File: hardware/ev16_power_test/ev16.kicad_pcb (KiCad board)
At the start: 4 copper layers, 125 x 80 mm, 185 parts, among them CN1 Conn_05x02_Female, CN2 PJ-242, J1 USB_C_Receptacle, J10 Conn_01x03_Pin, J11 Conn_02x05_Counter_Clockwise, J2 Conn_01x02_Socket, J3 AudioJack4, J4 Conn_02x03_Odd_Even, J5 Conn_02x03_Odd_Even, J6 Conn_02x05_Counter_Clockwise, J7 Conn_02x05_Counter_Clockwise, J8 Conn_02x05_Counter_Clockwise, J9 Conn_02x05_Counter_Clockwise, Q1 2N7002, Q2 2N7002, Q3 2N7002, SW1 SW_SPDT, SW2 SW_Push, SW3 SW_Push, SW4 SW_Push, SW5 SW_Push, SW6 SW_Push, SW7 SW_Push, U1 BQ21040DBV, U10 STM32F405RGTx, U11 ME6211C28M5, U2 USBLC6-2P6, U3 STM32F072CBTx, U4 CH340C, U5 TPS63060, U6 WM8960CGEFL/RV, U7 ESP32-S3-WROOM-1, U8 M24C02-RMN6TP, U9 TPS2116DRL, Y1 Crystal_GND24

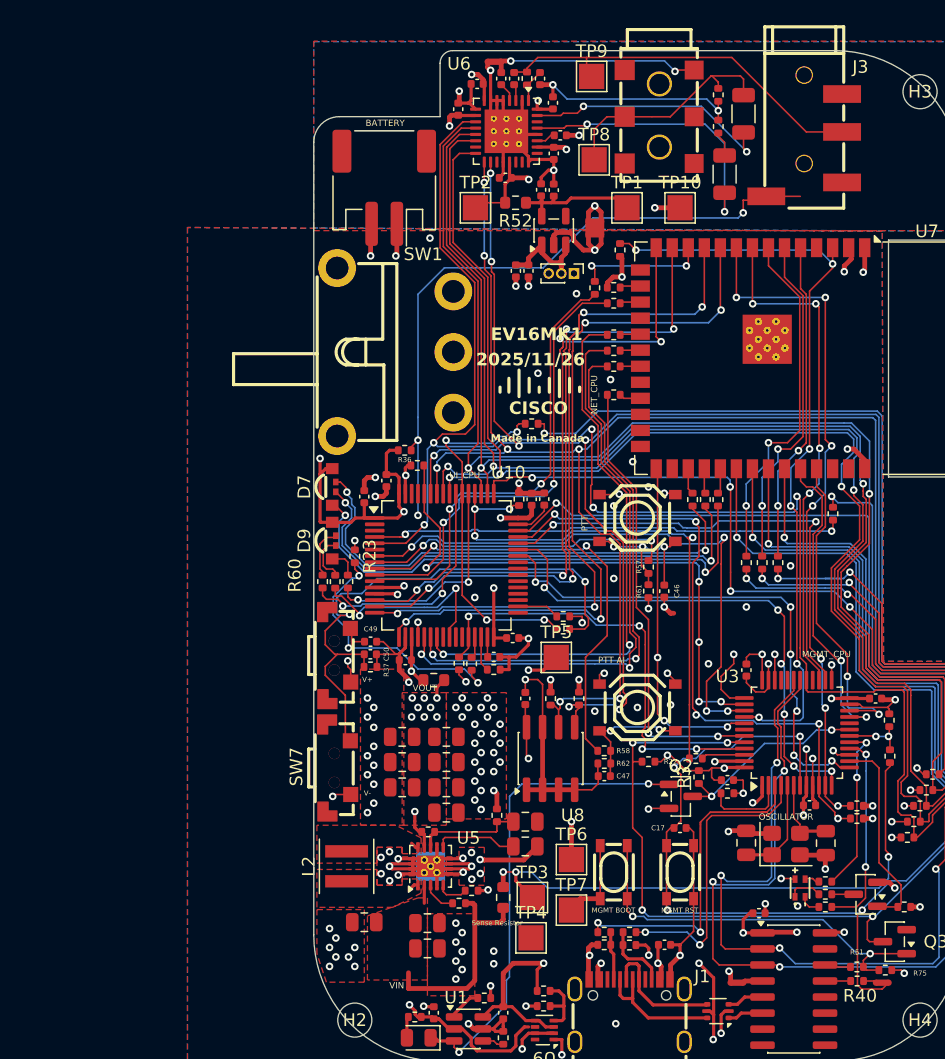
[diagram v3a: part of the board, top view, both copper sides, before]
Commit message: Changed linear regulator to XC6227C301MR-G and made a symbol for it. Added heat sink areas for the analog regulator
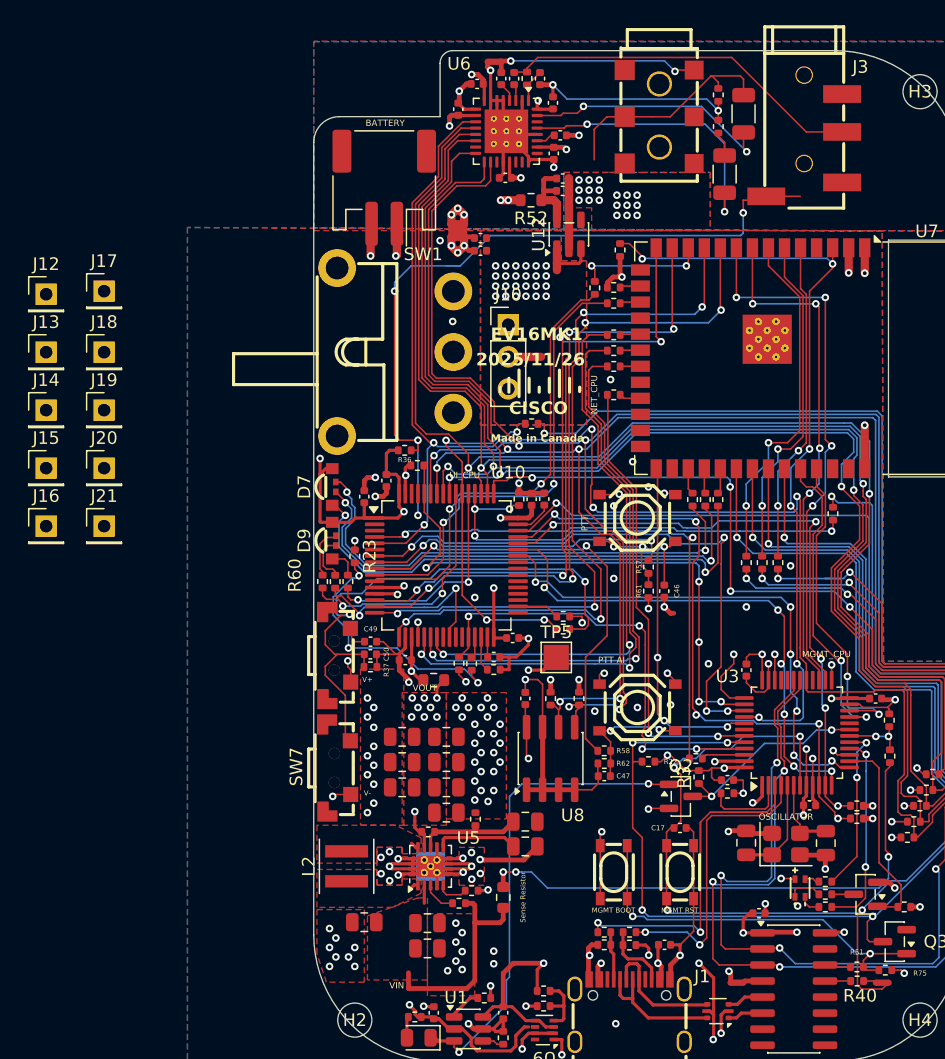
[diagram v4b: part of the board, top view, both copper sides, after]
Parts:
- removed TP1, TP10, TP2, TP3, TP4, TP6, TP7, TP8, TP9: TestPoint, TestPoint:TestPoint_Pad_2.0x2.0mm
- removed U11: ME6211C28M5, Package_TO_SOT_SMD:SOT-23-5
- added J12: Conn_01x01, Connector_PinHeader_2.54mm:PinHeader_1x01_P2.54mm_Vertical, F.Cu at (28.8, 49.3)
- added J13: Conn_01x01, Connector_PinHeader_2.54mm:PinHeader_1x01_P2.54mm_Vertical, F.Cu at (28.8, 53.9)
- added J14: Conn_01x01, Connector_PinHeader_2.54mm:PinHeader_1x01_P2.54mm_Vertical, F.Cu at (28.8, 58.5)
- added J15: Conn_01x01, Connector_PinHeader_2.54mm:PinHeader_1x01_P2.54mm_Vertical, F.Cu at (28.8, 63.0)
- added J16: Conn_01x01, Connector_PinHeader_2.54mm:PinHeader_1x01_P2.54mm_Vertical, F.Cu at (28.8, 67.6)
- added J17: Conn_01x01, Connector_PinHeader_2.54mm:PinHeader_1x01_P2.54mm_Vertical, F.Cu at (33.4, 49.0)
- added J18: Conn_01x01, Connector_PinHeader_2.54mm:PinHeader_1x01_P2.54mm_Vertical, F.Cu at (33.4, 53.9)
- added J19: Conn_01x01, Connector_PinHeader_2.54mm:PinHeader_1x01_P2.54mm_Vertical, F.Cu at (33.4, 58.5)
- added J20: Conn_01x01, Connector_PinHeader_2.54mm:PinHeader_1x01_P2.54mm_Vertical, F.Cu at (33.4, 63.0)
- added J21: Conn_01x01, Connector_PinHeader_2.54mm:PinHeader_1x01_P2.54mm_Vertical, F.Cu at (33.4, 67.6)
- added U12: XC6227C301MR-G, Package_TO_SOT_SMD:SOT-23-5, F.Cu at (70.2, 44.5)
- J10: footprint Connector_PinHeader_1.00mm:PinHeader_1x03_P1.00mm_Vertical -> Connector_PinHeader_2.54mm:PinHeader_1x03_P2.54mm_Vertical
- moved NT1 10.9 mm to (61.4, 44.2)
- moved J10 6.60 mm to (65.4, 51.7), turned to 0 degrees
- moved C7 4.12 mm to (63.2, 45.8), turned to 180 degrees
- moved C51 3.82 mm to (63.2, 44.8), turned to 180 degrees
- moved C18 1.93 mm to (69.7, 40.1), turned to 0 degrees
- moved R27 1.73 mm to (62.8, 90.8)
- moved R52 1.24 mm to (67.2, 41.8)
- moved C10 0.70 mm to (69.7, 41.1), turned to 0 degrees
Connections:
- net +3.3VA renamed +3.0VA
- net Net-(J10-Pin_2) renamed /AVIN
- C22 pad 1: Net-(U5-VOUT) -> Net-(J13-Pin_1)
- C24 pad 1: Net-(U5-VOUT) -> Net-(J13-Pin_1)
- C27 pad 1: Net-(U5-VOUT) -> Net-(J13-Pin_1)
- C29 pad 1: Net-(U5-VOUT) -> Net-(J13-Pin_1)
- C30 pad 1: Net-(U5-VOUT) -> Net-(J13-Pin_1)
- C31 pad 1: Net-(U5-VOUT) -> Net-(J13-Pin_1)
- C35 pad 1: Net-(U5-VOUT) -> Net-(J13-Pin_1)
- R26 pad 2: Net-(U5-VOUT) -> Net-(J13-Pin_1)
- R28 pad 2: Net-(U5-VOUT) -> Net-(J13-Pin_1)
- R48 pad 1: Net-(U5-VOUT) -> Net-(J13-Pin_1)
- U5 pad 9: Net-(U5-VOUT) -> Net-(J13-Pin_1)
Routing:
- net GND: track 299.5 -> 282.0 mm
- net Net-(U5-VOUT): track 26.1 -> 12.5 mm, vias 11 -> 1
- net Net-(J13-Pin_1): track 0.00 -> 13.5 mm, vias 0 -> 10
- net VSYS: track 117.0 -> 107.8 mm
- net GNDA: track 101.7 -> 93.1 mm, vias 7 -> 26
- net +3.3V: track 282.7 -> 275.2 mm, vias 35 -> 34
- net /UI_SDA1: track 141.3 -> 148.0 mm, vias 8 -> 6
- net /UI_SCL1: track 136.5 -> 142.9 mm, vias 8 -> 6
- net /MIC_IO: track 63.4 -> 69.7 mm, vias 4 -> 5
- net Net-(J20-Pin_1): track 10.8 -> 6.44 mm
- net /I2S_DACLRC: track 127.9 -> 131.4 mm
- net /I2S_DACDAT: track 117.8 -> 121.2 mm
- net /I2S_ADCDAT: track 121.5 -> 124.9 mm
- net /UI_TX2_NET: track 139.5 -> 137.0 mm
- net /I2S_BCLK: track 119.7 -> 121.9 mm
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- added copper zone on B.Cu, net /AVIN
- added copper zone on F.Cu, net /AVIN
- added copper zone on B.Cu, net GNDA
- added copper zone on F.Cu, net Net-(J13-Pin_1)
- removed copper zone on F.Cu, net Net-(U5-VOUT)
